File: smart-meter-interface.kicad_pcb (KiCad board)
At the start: 2 copper layers, 32 x 31.9 mm, 40 parts, among them J1 USB_B_Micro, Q1 PT26-21B/TR8, Q2 AO3400A, Q3 UMH3N, U2 ESP32-WROOM-32, U3 74LVC1G17DBVR, U4 CH340C

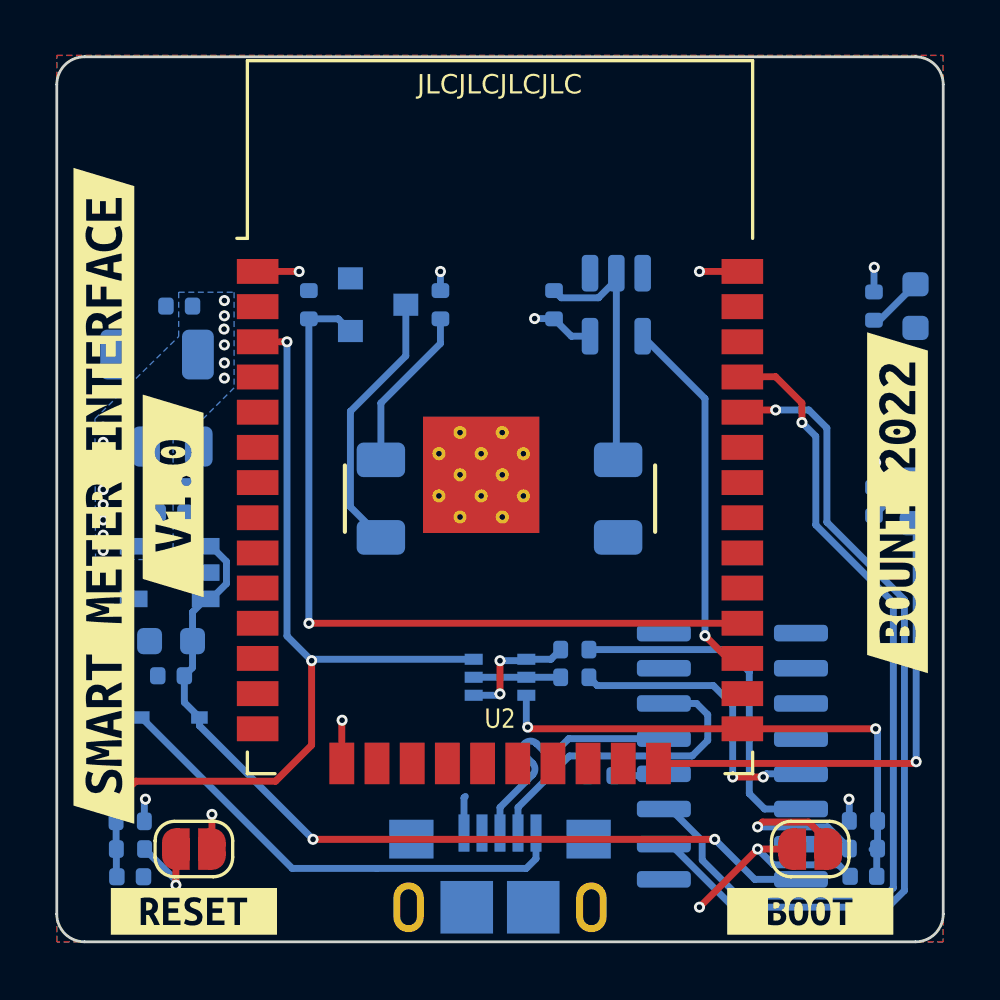
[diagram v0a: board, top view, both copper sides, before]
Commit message: Refactor to use Comperator instead of Schmitt Trigger
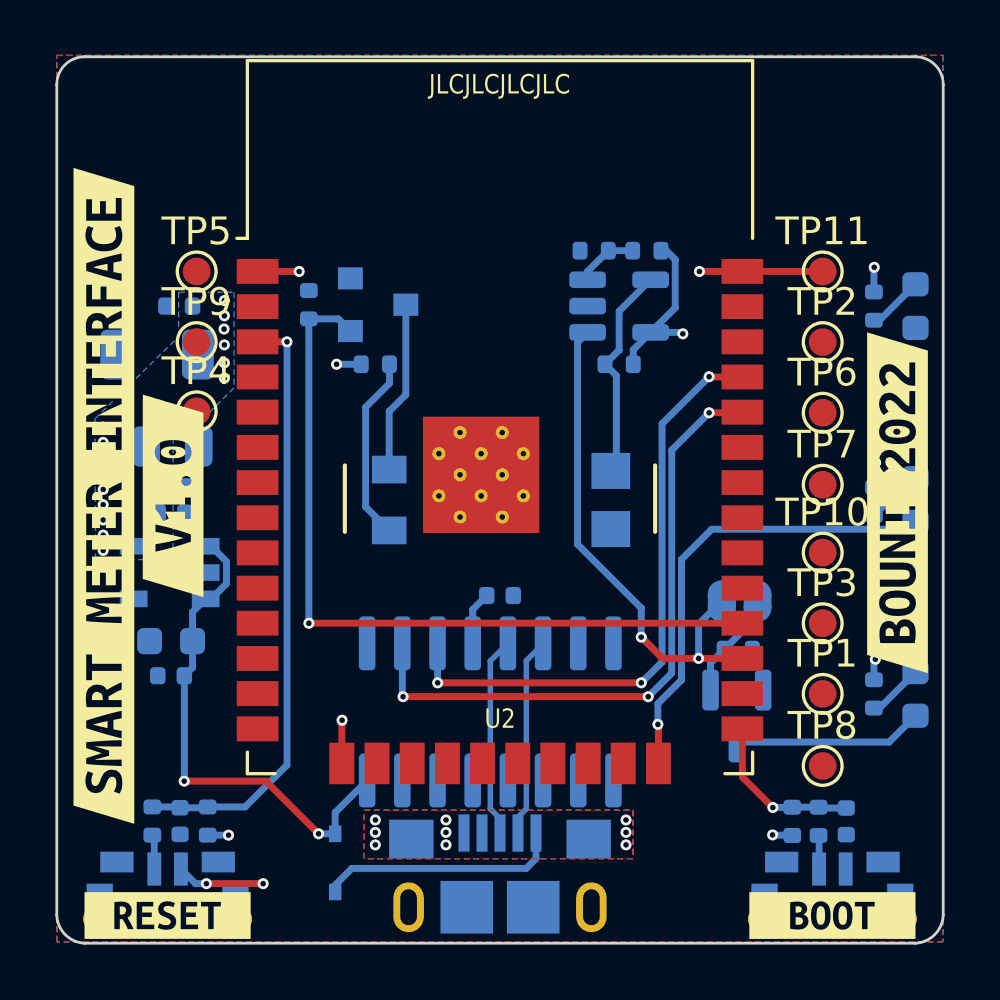
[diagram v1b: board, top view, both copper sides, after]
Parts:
- removed JP2: BOOT, Jumper:SolderJumper-2_P1.3mm_Open_RoundedPad1.0x1.5mm
- removed R2, R3: 1K, Resistor_SMD:R_0402_1005Metric
- added D5: LED, LED_SMD:LED_0603_1608Metric, B.Cu at (71.0, 63.0)
- added R12: 12k, Resistor_SMD:R_0402_1005Metric, B.Cu at (61.3, 47.0)
- added R13: 1k, Resistor_SMD:R_0402_1005Metric, B.Cu at (59.4, 47.0)
- added R14: 10k, Resistor_SMD:R_0402_1005Metric, B.Cu at (64.6, 61.4)
- added R15: 1k, Resistor_SMD:R_0402_1005Metric, B.Cu at (69.5, 63.0)
- added SW1: BOOT, LCSC:KEY-SMD_SKTGLBE010, B.Cu at (68.0, 70.1)
- added SW2: RESET, LCSC:KEY-SMD_SKTGLBE010, B.Cu at (44.0, 70.1)
- added TP1: TestPoint_Small, TestPoint:TestPoint_Pad_D1.0mm, F.Cu at (67.7, 63.0)
- added TP10: TestPoint_Small, TestPoint:TestPoint_Pad_D1.0mm, F.Cu at (67.7, 57.9)
- added TP11: TestPoint_Small, TestPoint:TestPoint_Pad_D1.0mm, F.Cu at (67.7, 47.8)
- added TP2: TestPoint_Small, TestPoint:TestPoint_Pad_D1.0mm, F.Cu at (67.7, 50.3)
- added TP3: TestPoint_Small, TestPoint:TestPoint_Pad_D1.0mm, F.Cu at (67.7, 60.5)
- added TP4: TestPoint_Small, TestPoint:TestPoint_Pad_D1.0mm, F.Cu at (45.0, 52.8)
- added TP5: TestPoint_Small, TestPoint:TestPoint_Pad_D1.0mm, F.Cu at (45.0, 47.8)
- added TP6: TestPoint_Small, TestPoint:TestPoint_Pad_D1.0mm, F.Cu at (67.7, 52.9)
- added TP7: TestPoint_Small, TestPoint:TestPoint_Pad_D1.0mm, F.Cu at (67.7, 55.5)
- added TP8: TestPoint_Small, TestPoint:TestPoint_Pad_D1.0mm, F.Cu at (67.7, 65.6)
- added TP9: TestPoint_Small, TestPoint:TestPoint_Pad_D1.0mm, F.Cu at (45.0, 50.3)
- D1: value IR26-21C/L110/CT -> XL-2012IRC-940; footprint LED_SMD:LED_1206_3216Metric -> LCSC:LED0805-RD
- JP1: value RESET -> SolderJumper_2_Open; moved to B.Cu
- Q1: value PT26-21B/TR8 -> PT17-21C/L41/TR8; footprint LED_SMD:LED_1206_3216Metric -> LCSC:OPTO-SMD_L2.0-W1.3-R-FD
- Q2: value AO3400A -> 2N7002
- Q3: value UMH3N -> 2N7002; footprint Package_TO_SOT_SMD:SOT-363_SC-70-6 -> Package_TO_SOT_SMD:SOT-23
- R1: value 10k -> 1k
- U3: value 74LVC1G17DBVR -> MCP6541T-I/OT
- moved JP1 9.31 mm to (64.7, 59.6)
- moved U4 8.89 mm to (55.6, 63.6), turned to -90 degrees
- moved Q3 8.66 mm to (64.5, 63.8), turned to -90 degrees
- moved D2 7.94 mm to (50.0, 69.1), turned to -90 degrees
- moved C1 7.45 mm to (56.0, 59.5), turned to 180 degrees
- moved R4 3.19 mm to (51.5, 51.1), turned to 0 degrees
- moved R1 3.19 mm to (60.3, 51.1), turned to 180 degrees
- moved R7 2.80 mm to (45.5, 67.6), turned to 90 degrees
- moved C10 2.70 mm to (44.5, 67.6), turned to 90 degrees
- moved R6 2.57 mm to (66.5, 67.6), turned to 90 degrees
- moved C9 2.08 mm to (68.5, 67.6), turned to 90 degrees
- moved R10 1.90 mm to (67.5, 67.6), turned to 90 degrees
- moved R11 1.28 mm to (43.5, 67.6), turned to 90 degrees
- moved kibuzzard-635BBBA9 0.96 mm to (44.0, 71.0)
- moved kibuzzard-635BBB9A 0.81 mm to (68.0, 71.0)
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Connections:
- JP1 pad 1: GND -> RX
- Q3 pad 1: RTS -> Net-(JP1-B)
- Q3 pad 2: DTR -> GND
- Q3 pad 3: IO0 -> Net-(D5-K)
- R10 pad 1: Net-(JP1-B) -> Net-(R10-Pad1)
- U3 pad 1: (no net) -> RX
- U3 pad 2: Net-(Q1-C) -> GND
- U3 pad 3: GND -> Net-(U3-+)
- U3 pad 4: RX -> Net-(Q1-C)
- U4 pad 13: Net-(U4-~{DTR}) -> unconnected-(U4-~{DTR})
- U4 pad 14: Net-(U4-~{RTS}) -> unconnected-(U4-~{RTS})
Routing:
- net +5V: track 31.9 -> 18.3 mm
- net IO0: track 19.1 -> 5.96 mm, vias 2 -> 1
- net Net-(U4-~{RTS}): track 12.6 -> 0.00 mm
- net Net-(U4-~{DTR}): track 10.7 -> 0.00 mm, vias 2 -> 0
- net EN: track 32.5 -> 21.9 mm, vias 3 -> 1
- net TXD0: track 31.5 -> 22.0 mm, vias 1 -> 3
- net Net-(D2-A): track 17.6 -> 8.82 mm
- net RXD0: track 31.1 -> 23.2 mm, vias 1 -> 3
- net Net-(D5-K): track 0.00 -> 6.84 mm
- net RX: track 13.4 -> 18.5 mm, vias 1 -> 2
- net +3V3: track 6.21 -> 11.1 mm, vias 21 -> 22
- net RTS: track 4.53 -> 0.00 mm, vias 2 -> 0
- net GND: track 15.2 -> 10.7 mm, vias 6 -> 14
- net /D-: track 11.5 -> 7.22 mm
- net Net-(D1-K): track 9.68 -> 6.20 mm
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- added copper zone on F.Cu, net GND
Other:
- board size 32 x 31.9 mm -> 32 x 32 mm
- board text added: "IO2"
- board text added: "PWR"
- board text added: "locked"
- board text removed: "TX"

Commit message: Final adjustments, next prototypes are ordered
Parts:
- removed TP10, TP8, TP9: TestPoint_Small, TestPoint:TestPoint_Pad_D1.0mm
- added JP2: SolderJumper_2_Open, Jumper:SolderJumper-2_P1.3mm_Open_RoundedPad1.0x1.5mm, B.Cu at (56.5, 48.0)
- added R16: 12k, Resistor_SMD:R_0402_1005Metric, B.Cu at (56.5, 50.0)
- added TP12: TestPoint_Small, TestPoint:TestPoint_Pad_D1.0mm, F.Cu at (45.0, 50.3)
- moved kibuzzard-635BBB71 16.8 mm to (56.0, 67.8), turned to 0 degrees
- moved TP1 2.60 mm to (67.7, 60.4)
- moved TP3 2.60 mm to (67.7, 57.9)
- moved TP6 2.60 mm to (67.7, 55.5)
- moved TP7 2.60 mm to (67.7, 52.9)
- moved TP4 0.10 mm to (45.0, 52.9)
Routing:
- net Net-(Q1-C): track 7.38 -> 16.6 mm, vias 0 -> 1
- net +5V: track 18.3 -> 27.0 mm, vias 2 -> 3
- net RX: track 18.5 -> 24.0 mm
- net RXD0: track 23.2 -> 27.8 mm
- net BLINK: track 28.3 -> 32.8 mm
- net TXD0: track 22.0 -> 25.5 mm
- net GND: track 10.7 -> 13.1 mm, vias 14 -> 15
- net Net-(JP2-A): track 2.24 -> 4.20 mm
- net Net-(JP2-B): track 0.00 -> 1.95 mm
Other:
- board text added: "3V3"
- board text added: "5V"
- board text added: "BL"
- board text added: "GND"
- board text added: "Q1"
- board text added: "RxD"
- board text added: "TxD"

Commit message: Major cleanup, hopefully working prototype orderd
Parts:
- removed D5: LED, LED_SMD:LED_0603_1608Metric
- removed JP1, JP2: SolderJumper_2_Open, Jumper:SolderJumper-2_P1.3mm_Open_RoundedPad1.0x1.5mm
- removed Q3: 2N7002, Package_TO_SOT_SMD:SOT-23
- removed R14: 10k, Resistor_SMD:R_0402_1005Metric
- removed R15: 1k, Resistor_SMD:R_0402_1005Metric
- removed U4: CH340C, Package_SO:SOIC-16_3.9x9.9mm_P1.27mm
- added REF**: OrderNumber, JLCPCB:OrderNumber, F.Cu at (56.0, 41.0)
- added TH1: ToolingHole, JLCPCB:ToolingHole, F.Cu at (41.5, 41.5)
- added TH2: ToolingHole, JLCPCB:ToolingHole, F.Cu at (70.5, 70.5)
- added U1: CH340E, Package_SO:MSOP-10_3x3mm_P0.5mm, B.Cu at (55.9, 63.6)
- R1: value 1k -> 10k
- R16: value 12k -> 12k DNP
- SW1, SW2: footprint LCSC:KEY-SMD_SKTGLBE010 -> LCSC:SW-SMD_4P-L5.1-W5.1-P3.70-LS6.5-TL-2
- kibuzzard-635BBB9A, kibuzzard-635BBBA9: moved to B.Cu
- moved R8 7.38 mm to (65.5, 55.2), turned to 0 degrees
- moved C9 6.09 mm to (62.5, 68.6)
- moved C10 5.36 mm to (49.7, 68.6)
- moved R11 5.36 mm to (48.7, 68.6)
- moved R7 5.36 mm to (50.7, 68.6)
- moved R6 5.15 mm to (61.5, 68.6)
- moved kibuzzard-635BBBA9 4.70 mm to (41.1, 67.3), turned to -90 degrees
- moved kibuzzard-635BBB9A 4.62 mm to (70.9, 67.4), turned to -90 degrees
- moved R10 4.12 mm to (63.5, 68.6)
- moved D2 4.10 mm to (50.0, 65.0)
- moved R13 4.02 mm to (63.3, 48.0), turned to 90 degrees
- moved R9 4.00 mm to (65.5, 56.2), turned to 0 degrees
- moved R1 3.58 mm to (57.4, 49.0), turned to 90 degrees
- moved R12 3.51 mm to (63.3, 49.9), turned to 90 degrees
- moved SW2 3.01 mm to (45.1, 67.3), turned to 90 degrees
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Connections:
- R12 pad 2: Net-(JP2-A) -> Net-(U3--)
- R13 pad 1: Net-(JP2-A) -> Net-(U3--)
- R16 pad 1: Net-(JP2-B) -> Net-(Q1-C)
- SW1 pad 1: GND -> Net-(R10-Pad1)
- SW1 pad 3: (no net) -> GND
- SW1 pad 4: (no net) -> GND
- SW2 pad 1: GND -> Net-(R11-Pad1)
- SW2 pad 3: (no net) -> GND
- SW2 pad 4: (no net) -> GND
- U3 pad 3: Net-(JP2-A) -> Net-(Q1-C)
- U3 pad 4: Net-(Q1-C) -> Net-(U3--)
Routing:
- net +3V3: track 11.1 -> 58.9 mm, vias 22 -> 7
- net GND: track 13.1 -> 4.64 mm, vias 15 -> 49
- net Net-(D3-A): track 2.04 -> 10.2 mm
- net Net-(R11-Pad1): track 1.25 -> 8.87 mm
- net Net-(R10-Pad1): track 1.22 -> 8.77 mm
- net Net-(D5-K): track 6.84 -> 0.00 mm
- net Net-(JP2-A): track 4.20 -> 0.00 mm
- net Net-(JP1-B): track 3.92 -> 0.00 mm
- net Net-(D4-A): track 1.89 -> 5.41 mm
- net Net-(U3--): track 0.00 -> 2.93 mm
- net RX: track 24.0 -> 26.3 mm, vias 2 -> 3
- net Net-(D5-A): track 2.04 -> 0.00 mm
- net Net-(JP2-B): track 1.95 -> 0.00 mm
- net Net-(Q1-C): track 16.6 -> 18.6 mm, vias 1 -> 3
- net IO2: track 16.6 -> 18.1 mm
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- removed copper zone on F.Cu, net +3V3
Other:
- board text removed: "JLCJLCJLCJLC"

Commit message: Fixed last issues
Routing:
- net GND: vias 49 -> 46
